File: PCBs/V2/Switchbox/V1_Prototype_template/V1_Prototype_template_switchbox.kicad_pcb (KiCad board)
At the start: 2 copper layers, 9 parts, among them J1 Conn_02x10_Top_Bottom, J2 Conn_02x10_Top_Bottom

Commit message: progress on switchboard schematic
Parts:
- added J3(IN)1: 5360, FootprintLibrary:5360, F.Cu at (65.9, 92.0)
- added J5(OUT)1: 5360, FootprintLibrary:5360, F.Cu at (65.9, 101.5)
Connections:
- J2 pad 11: /GND -> /VCC
- J2 pad 12: /GND -> /VCC
- J2 pad 13: /GND -> /VCC
- J2 pad 14: /GND -> /VCC
- J2 pad 15: /GND -> /VCC
- J2 pad 16: /GND -> /VCC
- J2 pad 17: /GND -> /VCC
- J2 pad 18: /GND -> /VCC
- J2 pad 19: /GND -> /VCC
- J2 pad 20: /GND -> /VCC

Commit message: good progress on switchbox pcb design
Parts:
- removed UART1(COMS)1: Conn_01x02_Pin, Connector_PinHeader_2.54mm:PinHeader_1x02_P2.54mm_Vertical
- added J3: Conn_02x10_Top_Bottom, Connector_PinHeader_1.00mm:PinHeader_2x10_P1.00mm_Vertical, F.Cu at (101.5, 89.5)
- J3(IN)1, J5(OUT)1: value 5360 -> 01x04 magnetic connector; footprint FootprintLibrary:5360 -> FootprintLibrary:5358_4pin_connector_customfootprint
- leave open: renamed from Leave_Open1
- moved J3(IN)1 49.6 mm to (115.5, 91.0), turned to 90 degrees
- moved J2 22.9 mm to (109.5, 89.5), turned to 180 degrees
- moved 1k1 20.6 mm to (91.1, 93.0)
- moved 1k2 20.6 mm to (91.1, 95.5)
- moved leave open 20.6 mm to (91.1, 98.0)
- moved J1 17.0 mm to (105.5, 89.5), turned to 180 degrees
- moved J5(OUT)1 14.4 mm to (76.5, 91.8), turned to -90 degrees
- moved Programmer 12.9 mm to (83.5, 82.9)
- moved STM32L031K6Tx1 7.32 mm to (91.7, 86.2)
- moved Reset1 6.26 mm to (87.5, 95.0), turned to -90 degrees
- renumbered Programmer1 to Programmer
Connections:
- J2 pad 11: /VCC -> /GND
- J2 pad 12: /VCC -> /GND
- J2 pad 13: /VCC -> /GND
- J2 pad 14: /VCC -> /GND
- J2 pad 15: /VCC -> /GND
- J2 pad 16: /VCC -> /GND
- J2 pad 17: /VCC -> /GND
- J2 pad 18: /VCC -> /GND
- J2 pad 19: /VCC -> /GND
- J2 pad 20: /VCC -> /GND
- J3(IN)1 pad 1: /UART_RX(PA10) -> /GND
- J3(IN)1 pad 2: /UART_TX(PA9) -> /VCC
- J3(IN)1 pad 3: /GND -> /UART_TX(PA9)
- J5(OUT)1 pad 1: /UART_TX(PA9) -> /GND
- J5(OUT)1 pad 2: /UART_RX(PA10) -> /VCC
- J5(OUT)1 pad 3: /GND -> /UART_RX(PA10)
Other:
- board outline added: 48 x 28 mm

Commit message: PCB For switchbox prototype done
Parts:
- removed J1, J2, J3: Conn_02x10_Top_Bottom, Connector_PinHeader_1.00mm:PinHeader_2x10_P1.00mm_Vertical
- removed Programmer: Conn_01x04, Connector_PinHeader_2.54mm:PinHeader_1x04_P2.54mm_Vertical
- removed leave open: R, Resistor_SMD:R_0603_1608Metric_Pad0.98x0.95mm_HandSolder
- added Leave_Open1: R, Resistor_SMD:R_0603_1608Metric_Pad0.98x0.95mm_HandSolder, F.Cu at (94.0, 82.5)
- added Programmer1: Conn_01x04, Connector_PinHeader_2.54mm:PinHeader_1x04_P2.54mm_Vertical, F.Cu at (83.0, 80.5)
- added U1: ~, FootprintLibrary:PinHeader_03x20, F.Cu at (130.6, 62.4)
- moved J5(OUT)1 63.5 mm to (138.0, 76.0), turned to 90 degrees
- moved J3(IN)1 42.0 mm to (76.0, 76.8), turned to -90 degrees
- moved 1k2 15.8 mm to (98.5, 81.5), turned to 90 degrees
- moved 1k1 13.3 mm to (86.5, 80.5), turned to -90 degrees
- moved STM32L031K6Tx1 10.8 mm to (93.5, 75.5), turned to 180 degrees
- moved Reset1 5.70 mm to (89.0, 89.5), turned to 180 degrees
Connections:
- J5(OUT)1 pad 1: /GND -> /UART_TX(PA9)
- J5(OUT)1 pad 2: /VCC -> /UART_RX(PA10)
- J5(OUT)1 pad 3: /UART_RX(PA10) -> /VCC
- J5(OUT)1 pad 4: /UART_TX(PA9) -> /GND
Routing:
- net /VCC: track 0.00 -> 169.3 mm, vias 0 -> 6
- net /UART_TX(PA9): track 0.00 -> 87.0 mm, vias 0 -> 3
- net /UART_RX(PA10): track 0.00 -> 76.9 mm, vias 0 -> 3
- net /PB7: track 0.00 -> 38.9 mm, vias 0 -> 1
- net /PB6: track 0.00 -> 37.6 mm, vias 0 -> 1
- net /PB5: track 0.00 -> 36.2 mm, vias 0 -> 1
- net /PB4: track 0.00 -> 34.6 mm, vias 0 -> 1
- net /PB3: track 0.00 -> 33.0 mm, vias 0 -> 1
- net Net-(STM32L031K6Tx1-NRST): track 0.00 -> 32.7 mm
- net /PA15: track 0.00 -> 32.0 mm, vias 0 -> 1
- net /PA12: track 0.00 -> 27.3 mm, vias 0 -> 1
- net /PA11: track 0.00 -> 24.5 mm, vias 0 -> 1
- net /PA8: track 0.00 -> 20.9 mm, vias 0 -> 1
- net /GND: track 0.00 -> 16.6 mm, vias 0 -> 43
- net /PB1: track 0.00 -> 12.3 mm
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- added copper zone on B.Cu, net /GND
- added copper zone on F.Cu, net /GND
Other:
- board size 48 x 28 mm -> 70 x 35 mm

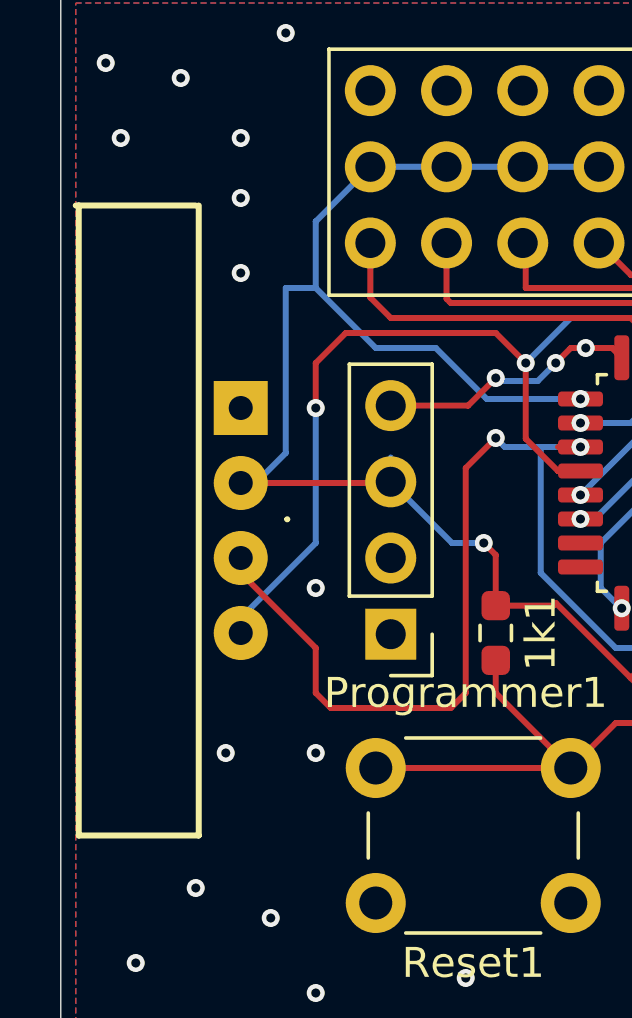
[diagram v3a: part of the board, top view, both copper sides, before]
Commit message: fixed connector heights on switchbox pcb
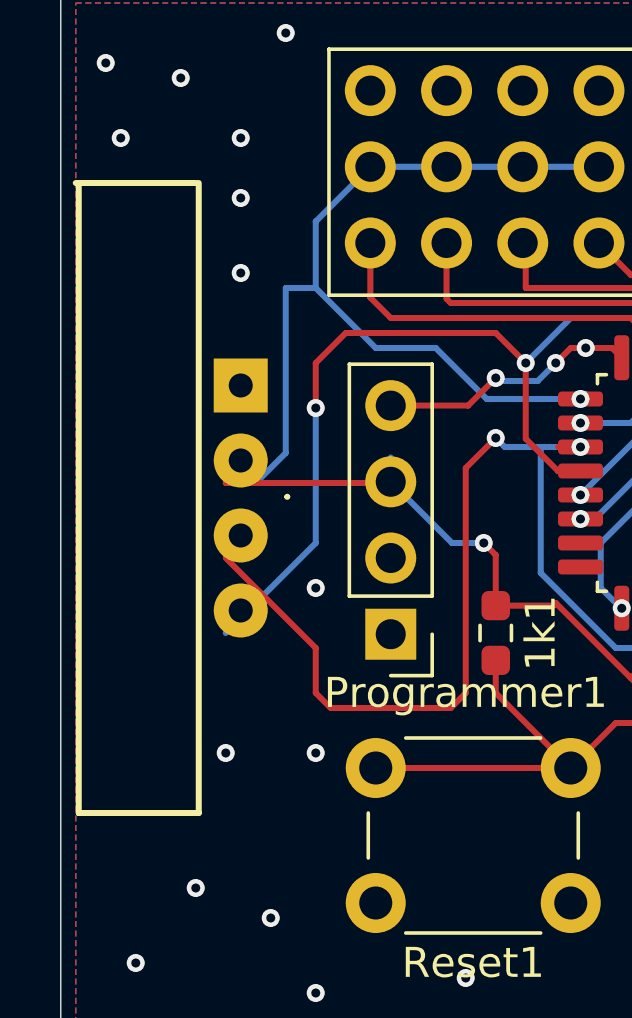
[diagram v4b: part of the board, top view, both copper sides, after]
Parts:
- moved J3(IN)1 0.75 mm to (76.0, 76.0)
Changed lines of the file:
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@@
 		)
 		(property "Value" "01x04 magnetic connector"
-			(at 0 0.9 90)
+			(at -0.5 0 90)
 			(unlocked yes)
 			(layer "F.Fab")
@@
 	(footprint "FootprintLibrary:5358_4pin_connector_customfootprint"
 		(layer "F.Cu")
-		(at 76 76.75 -90)
+		(at 76 76 -90)
 		(property "Reference" "J3(IN)1"
 			(at 0 -1 270)
@@
 		)
 		(property "Value" "01x04 magnetic connector"
-			(at 0 0.9 270)
-			(unlocked yes)
-			(layer "F.Fab")
+			(at 0 -0.5 270)
+			(unlocked yes)
+			(layer "F.Fab")

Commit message: small fixes to switchbox pcb
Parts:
- moved Programmer1 0.08 mm to (83.0, 80.6)
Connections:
- Programmer1 pad 1: /SWCLK -> /SWDIO(PA13)
- Programmer1 pad 2: /SWDIO -> /SWCLK(PA14)
- STM32L031K6Tx1 pad 23: /SWCLK(PA13) -> /SWDIO(PA13)
- STM32L031K6Tx1 pad 24: /SWDIO(PA14) -> /SWCLK(PA14)
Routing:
- net /SWCLK(PA14): track 0.00 -> 8.97 mm, vias 0 -> 2
- net /SWDIO(PA13): track 0.00 -> 8.40 mm, vias 0 -> 1
- net /UART_TX(PA9): track 87.0 -> 87.6 mm

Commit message: some updates
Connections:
- net /UART_RX(PA10) renamed /USART_RX(PA10)
- net /UART_TX(PA9) renamed /USART_TX(PA9)
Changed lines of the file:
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@@
 	(net 26 "/SWCLK(PA14)")
 	(net 27 "/PC15")
-	(net 28 "/UART_TX(PA9)")
-	(net 29 "/UART_RX(PA10)")
+	(net 28 "/USART_TX(PA9)")
+	(net 29 "/USART_RX(PA10)")
 	(net 30 "unconnected-(U1-Pad3)")
 	(footprint "Resistor_SMD:R_0603_1608Metric_Pad0.98x0.95mm_HandSolder"
@@
 			(layers "*.Cu" "*.Mask")
 			(remove_unused_layers no)
-			(net 28 "/UART_TX(PA9)")
+			(net 28 "/USART_TX(PA9)")
 			(pinfunction "Pin_1")
 			(pintype "passive")
@@
 			(layers "*.Cu" "*.Mask")
 			(remove_unused_layers no)
-			(net 29 "/UART_RX(PA10)")
+			(net 29 "/USART_RX(PA10)")
 			(pinfunction "Pin_2")
 			(pintype "passive")
@@
 			(layers "*.Cu" "*.Mask")
 			(remove_unused_layers no)
-			(net 28 "/UART_TX(PA9)")
+			(net 28 "/USART_TX(PA9)")
 			(pinfunction "Pin_3")
 			(pintype "passive")
@@
 			(layers "*.Cu" "*.Mask")
 			(remove_unused_layers no)
-			(net 29 "/UART_RX(PA10)")
+			(net 29 "/USART_RX(PA10)")
 			(pinfunction "Pin_4")
 			(pintype "passive")
@@
 			(layers "F.Cu" "F.Mask" "F.Paste")
 			(roundrect_rratio 0.25)
-			(net 28 "/UART_TX(PA9)")
+			(net 28 "/USART_TX(PA9)")
 			(pinfunction "PA9")
 			(pintype "bidirectional")
@@
 			(layers "F.Cu" "F.Mask" "F.Paste")
 			(roundrect_rratio 0.25)
-			(net 29 "/UART_RX(PA10)")
+			(net 29 "/USART_RX(PA10)")
 			(pinfunction "PA10")
 			(pintype "bidirectional")

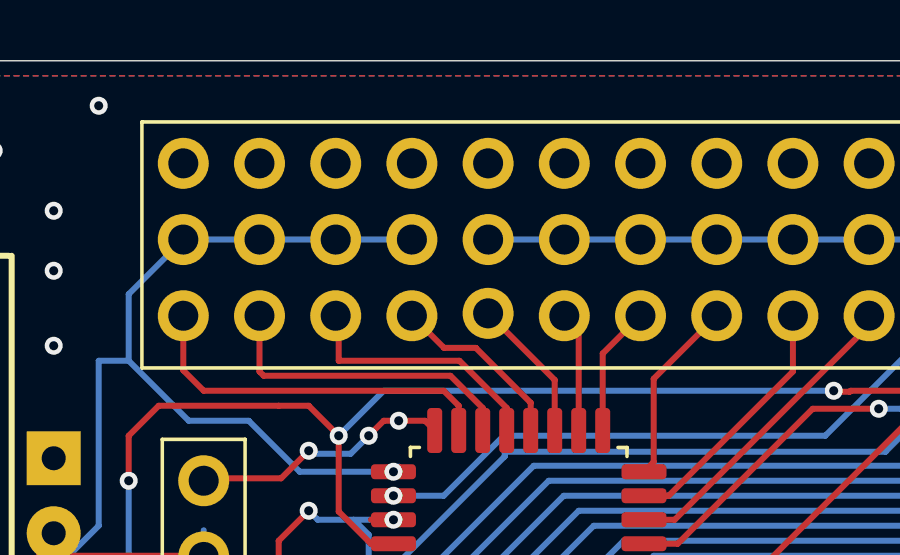
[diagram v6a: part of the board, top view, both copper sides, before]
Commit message: messed UART connection for synthesis PCB :/ good thing i had those misc pads for testing. Need to reorder.
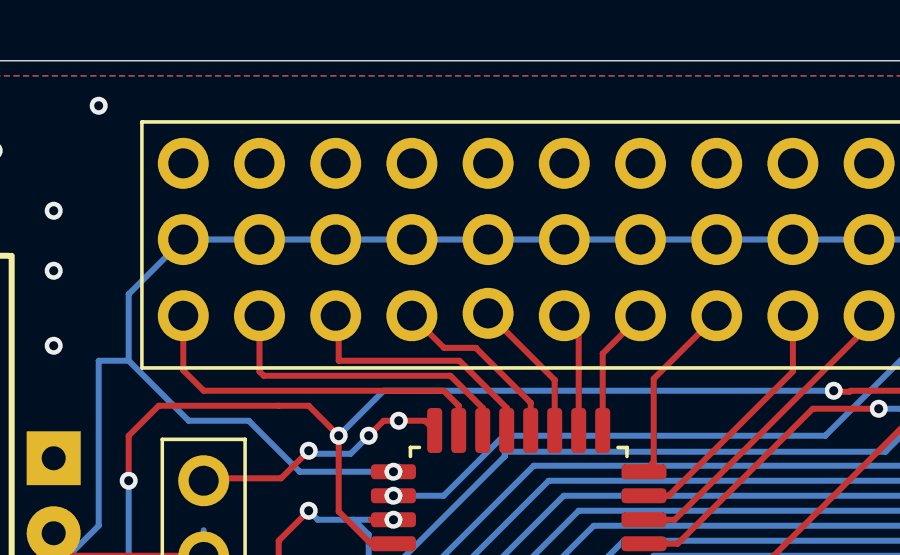
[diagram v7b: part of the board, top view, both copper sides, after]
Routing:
- net /VCC: track 169.3 -> 171.8 mm
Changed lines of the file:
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@@
+	)
+	(segment
+		(start 89.94 64.96)
+		(end 92.48 64.96)
+		(width 0.2)
+		(layer "B.Cu")
+		(net 2)
 	)
 	(segment

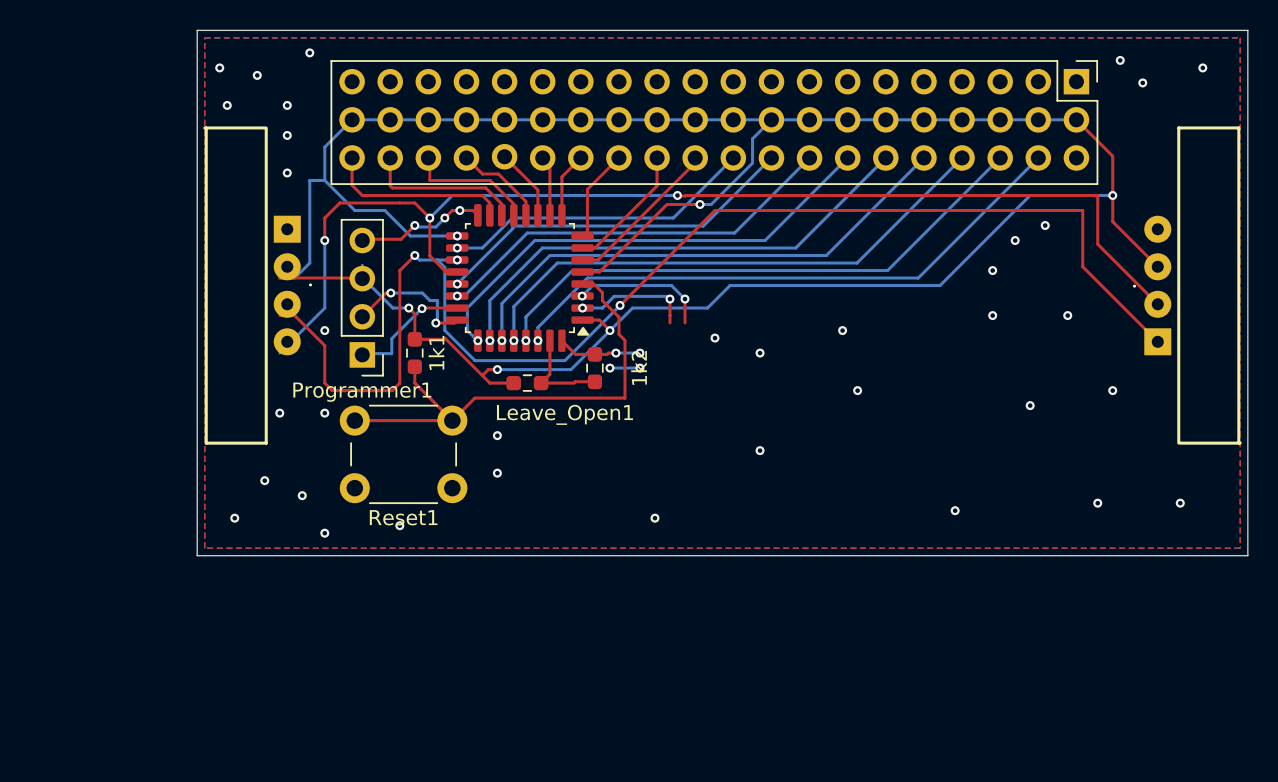
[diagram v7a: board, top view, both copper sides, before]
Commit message: Switchbox pcb was also fucked up, fixed that, need to order now. (and tweaked the switchbox boilerplate code.
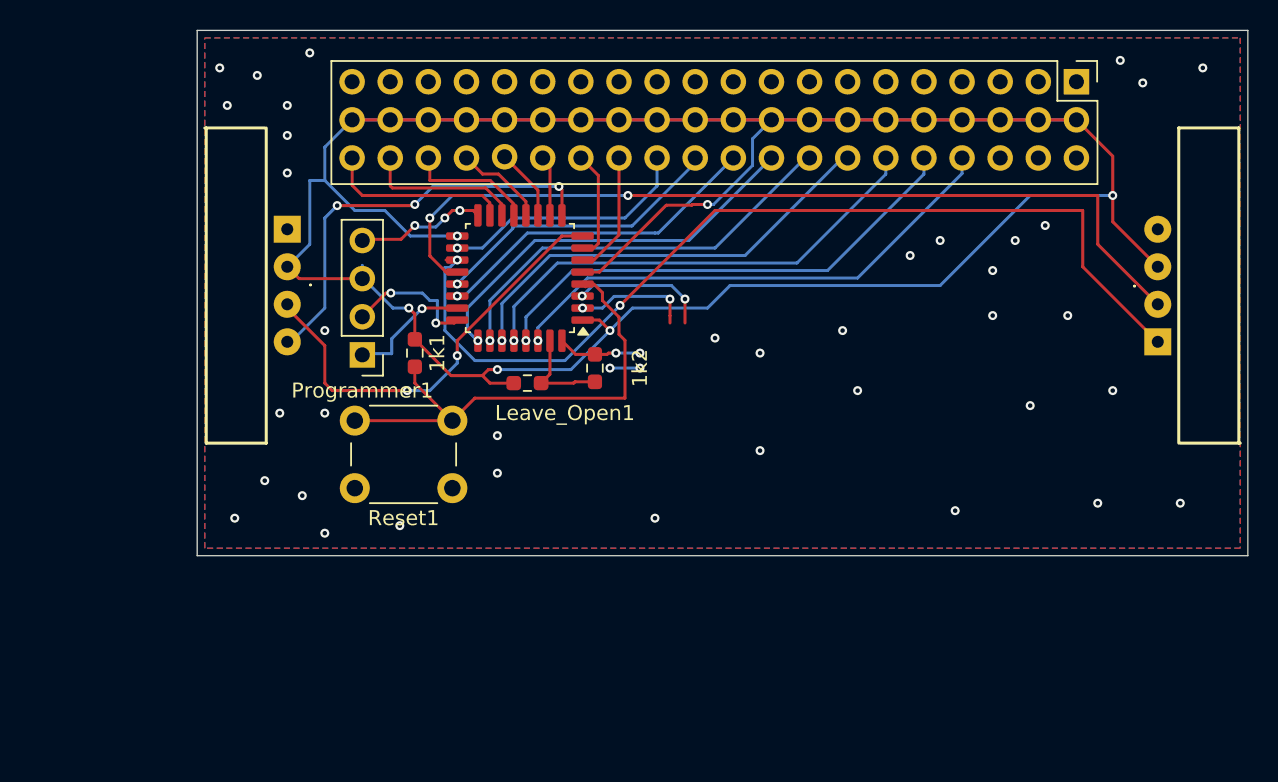
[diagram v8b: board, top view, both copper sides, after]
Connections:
- J3(IN)1 pad 3: /USART_TX(PA9) -> /PREV_LPUART1_TX(PA2)
- J3(IN)1 pad 4: /USART_RX(PA10) -> /PREV_LPUART1_RX(PA3)
- J5(OUT)1 pad 1: /USART_TX(PA9) -> /NEXT_USART2_TX(PA9)
- J5(OUT)1 pad 2: /USART_RX(PA10) -> /NEXT_USART2_RX(PA10)
- STM32L031K6Tx1 pad 19: /USART_TX(PA9) -> /NEXT_USART2_TX(PA9)
- STM32L031K6Tx1 pad 20: /USART_RX(PA10) -> /NEXT_USART2_RX(PA10)
- STM32L031K6Tx1 pad 8: /PA2 -> /PREV_LPUART1_TX(PA2)
- STM32L031K6Tx1 pad 9: /PA3 -> /PREV_LPUART1_RX(PA3)
- U1 pad 12: /PB5 -> /PB7
- U1 pad 15: /PB4 -> /PB6
- U1 pad 18: /PB3 -> /PB5
- U1 pad 21: /PA15 -> /PB4
- U1 pad 24: /PA12 -> /PB3
- U1 pad 27: /PA11 -> /PA15
- U1 pad 30: /PA8 -> /PA12
- U1 pad 33: /PA0 -> /PA11
- U1 pad 36: /PA1 -> /PA8
- U1 pad 39: /PA2 -> /PA0
- U1 pad 42: /PA3 -> /PA1
- U1 pad 6: /PB7 -> unconnected-(U1-Pad6)
- U1 pad 9: /PB6 -> unconnected-(U1-Pad9)
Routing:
- net /USART_TX(PA9): track 87.6 -> 0.00 mm, vias 3 -> 0
- net /USART_RX(PA10): track 76.9 -> 0.00 mm, vias 3 -> 0
- net /NEXT_USART2_TX(PA9): track 0.00 -> 64.3 mm, vias 0 -> 2
- net /NEXT_USART2_RX(PA10): track 0.00 -> 58.8 mm, vias 0 -> 2
- net /VCC: track 171.8 -> 218.4 mm
- net /PREV_LPUART1_TX(PA2): track 0.00 -> 28.8 mm, vias 0 -> 2
- net /PREV_LPUART1_RX(PA3): track 0.00 -> 27.9 mm, vias 0 -> 3
- net /PA2: track 6.20 -> 0.00 mm
- net /PB4: track 34.6 -> 29.5 mm
- net /PB3: track 33.0 -> 27.9 mm
- net /PA15: track 32.0 -> 26.9 mm
- net /PA12: track 27.3 -> 22.2 mm
- net /PA11: track 24.5 -> 19.9 mm
- net /PB7: track 38.9 -> 34.4 mm
- net /PB5: track 36.2 -> 31.8 mm
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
